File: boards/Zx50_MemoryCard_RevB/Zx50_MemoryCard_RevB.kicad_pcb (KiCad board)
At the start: 4 copper layers, 132.1 x 107.9 mm, 115 parts, among them J1 3.3V, J10 DEBUG, J2 Zx50_EdgeConnector, J3 TP_CLK, J4 TP_MCLK, J5 GND, J6 GND, J7 GND, J8 JTAG, J9 RJ45_RB1-125B8G1A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

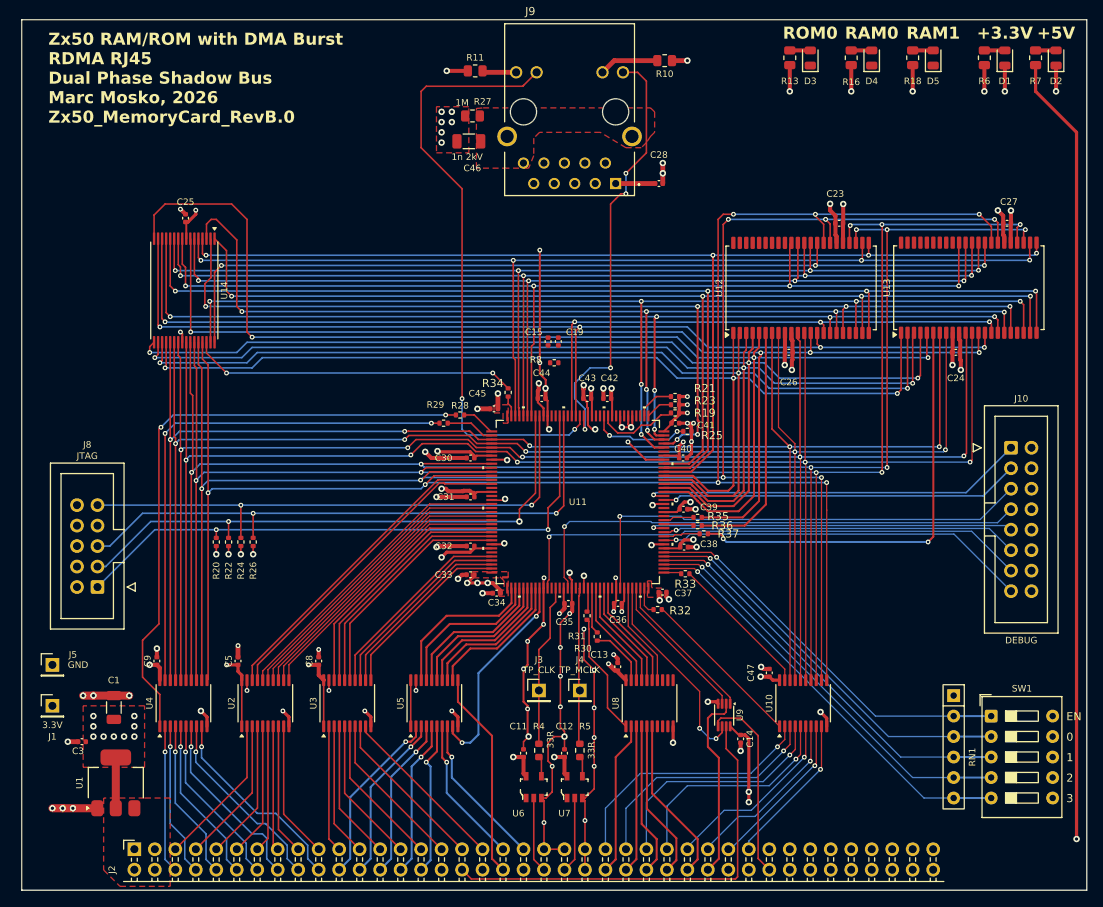
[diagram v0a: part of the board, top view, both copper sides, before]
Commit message: tweeks before refitting with quartus
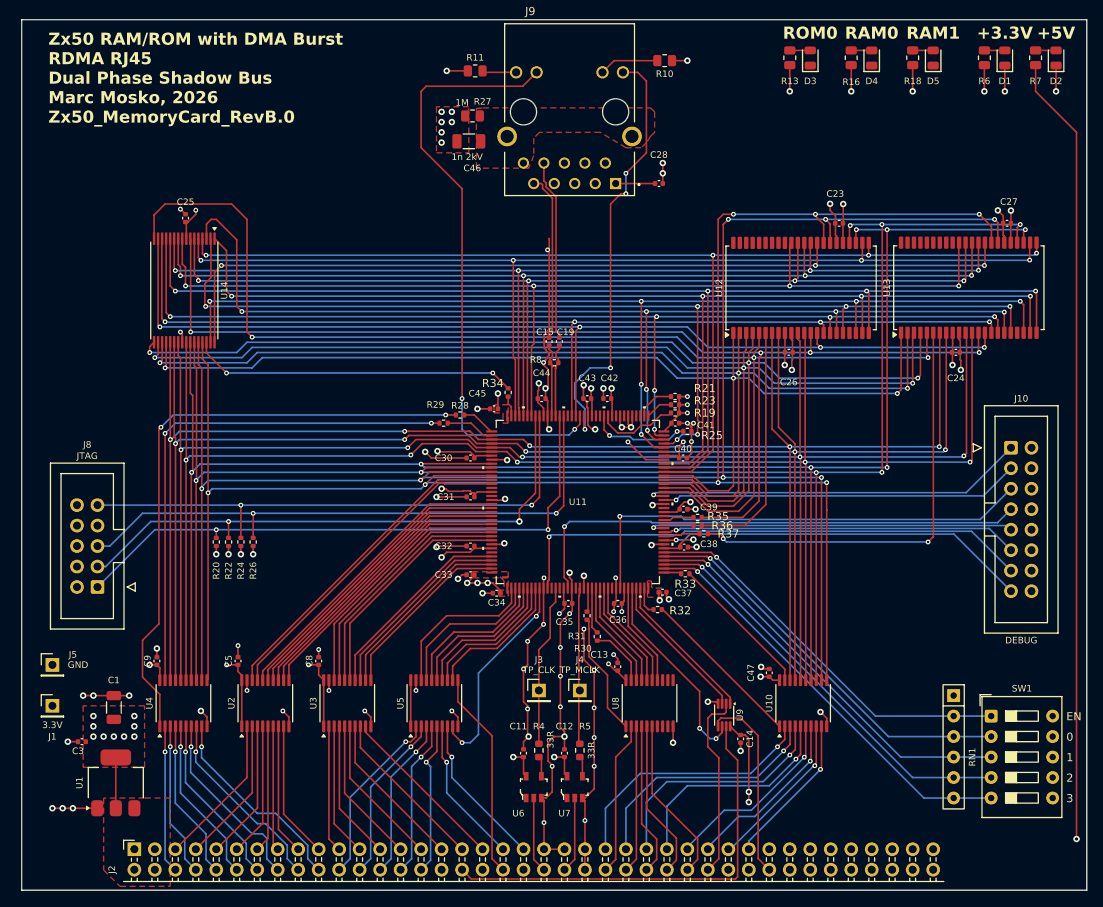
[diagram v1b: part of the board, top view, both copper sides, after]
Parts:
- moved C15 1.40 mm to (98.4, 97.1)
- moved C19 1.14 mm to (97.2, 97.1)
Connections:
- C15 pad 1: /FPGA And Memory/RX_CLK_FLT_N -> /FPGA And Memory/RX_CLK_FLT_P
- C15 pad 2: /FPGA And Memory/RX_CLK_N -> /FPGA And Memory/RX_CLK_P
- C19 pad 1: /FPGA And Memory/RX_CLK_FLT_P -> /FPGA And Memory/RX_CLK_FLT_N
- C19 pad 2: /FPGA And Memory/RX_CLK_P -> /FPGA And Memory/RX_CLK_N
- R8 pad 1: /FPGA And Memory/RX_CLK_FLT_N -> /FPGA And Memory/RX_CLK_FLT_P
- R8 pad 2: /FPGA And Memory/RX_CLK_FLT_P -> /FPGA And Memory/RX_CLK_FLT_N
- U11 pad 132: /FPGA And Memory/RX_CLK_FLT_N -> /FPGA And Memory/RX_CLK_FLT_P
- U11 pad 133: /FPGA And Memory/RX_CLK_FLT_P -> /FPGA And Memory/RX_CLK_FLT_N
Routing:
- net /FPGA And Memory/RX_CLK_P: track 0.00 -> 22.4 mm
- net /FPGA And Memory/RX_CLK_N: track 0.00 -> 20.8 mm
- net /FPGA And Memory/RX_CLK_FLT_P: track 0.00 -> 9.11 mm
- net /FPGA And Memory/RX_CLK_FLT_N: track 0.00 -> 9.11 mm
- net GND: track 247.8 -> 250.2 mm
- net +3.3V: track 156.0 -> 155.1 mm

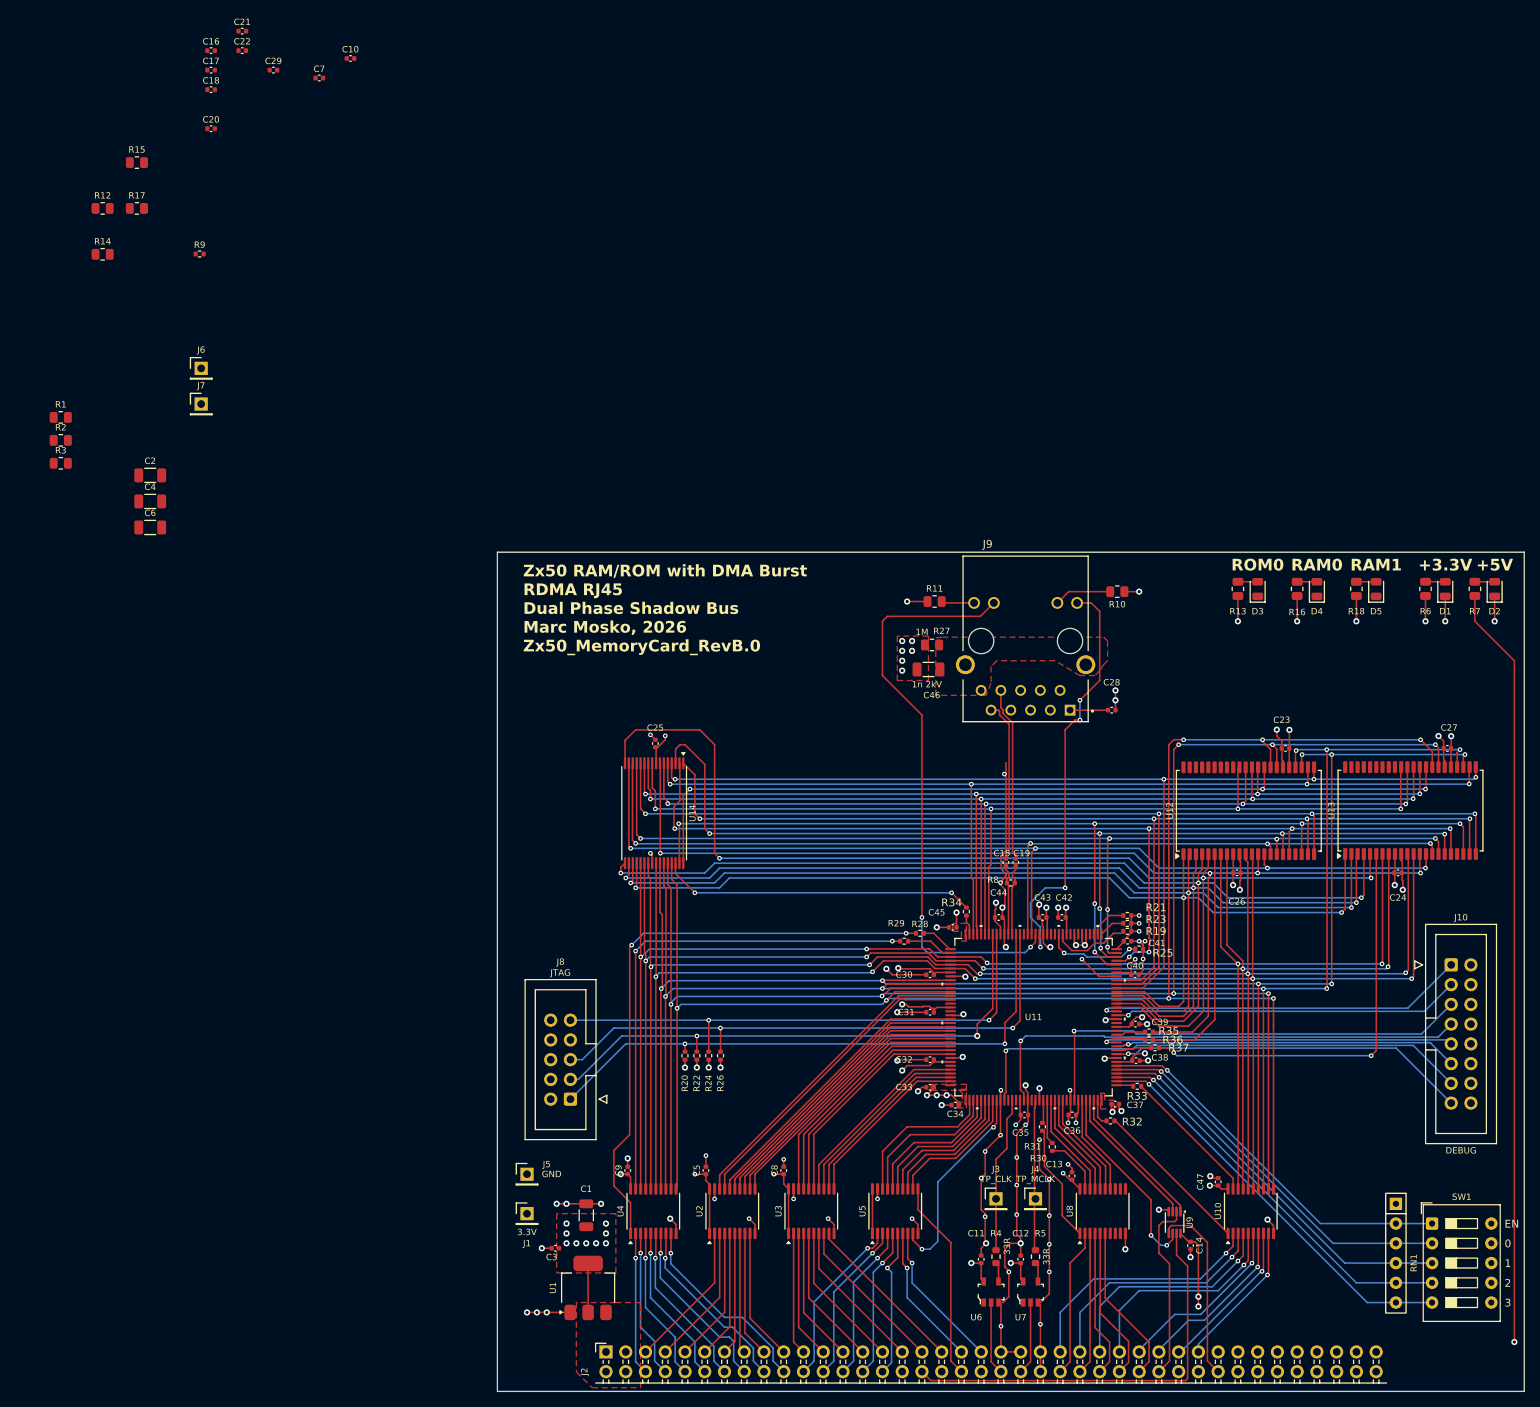
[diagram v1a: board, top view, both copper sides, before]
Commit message: more work on revb memory card, plus a diag program for rev a1.
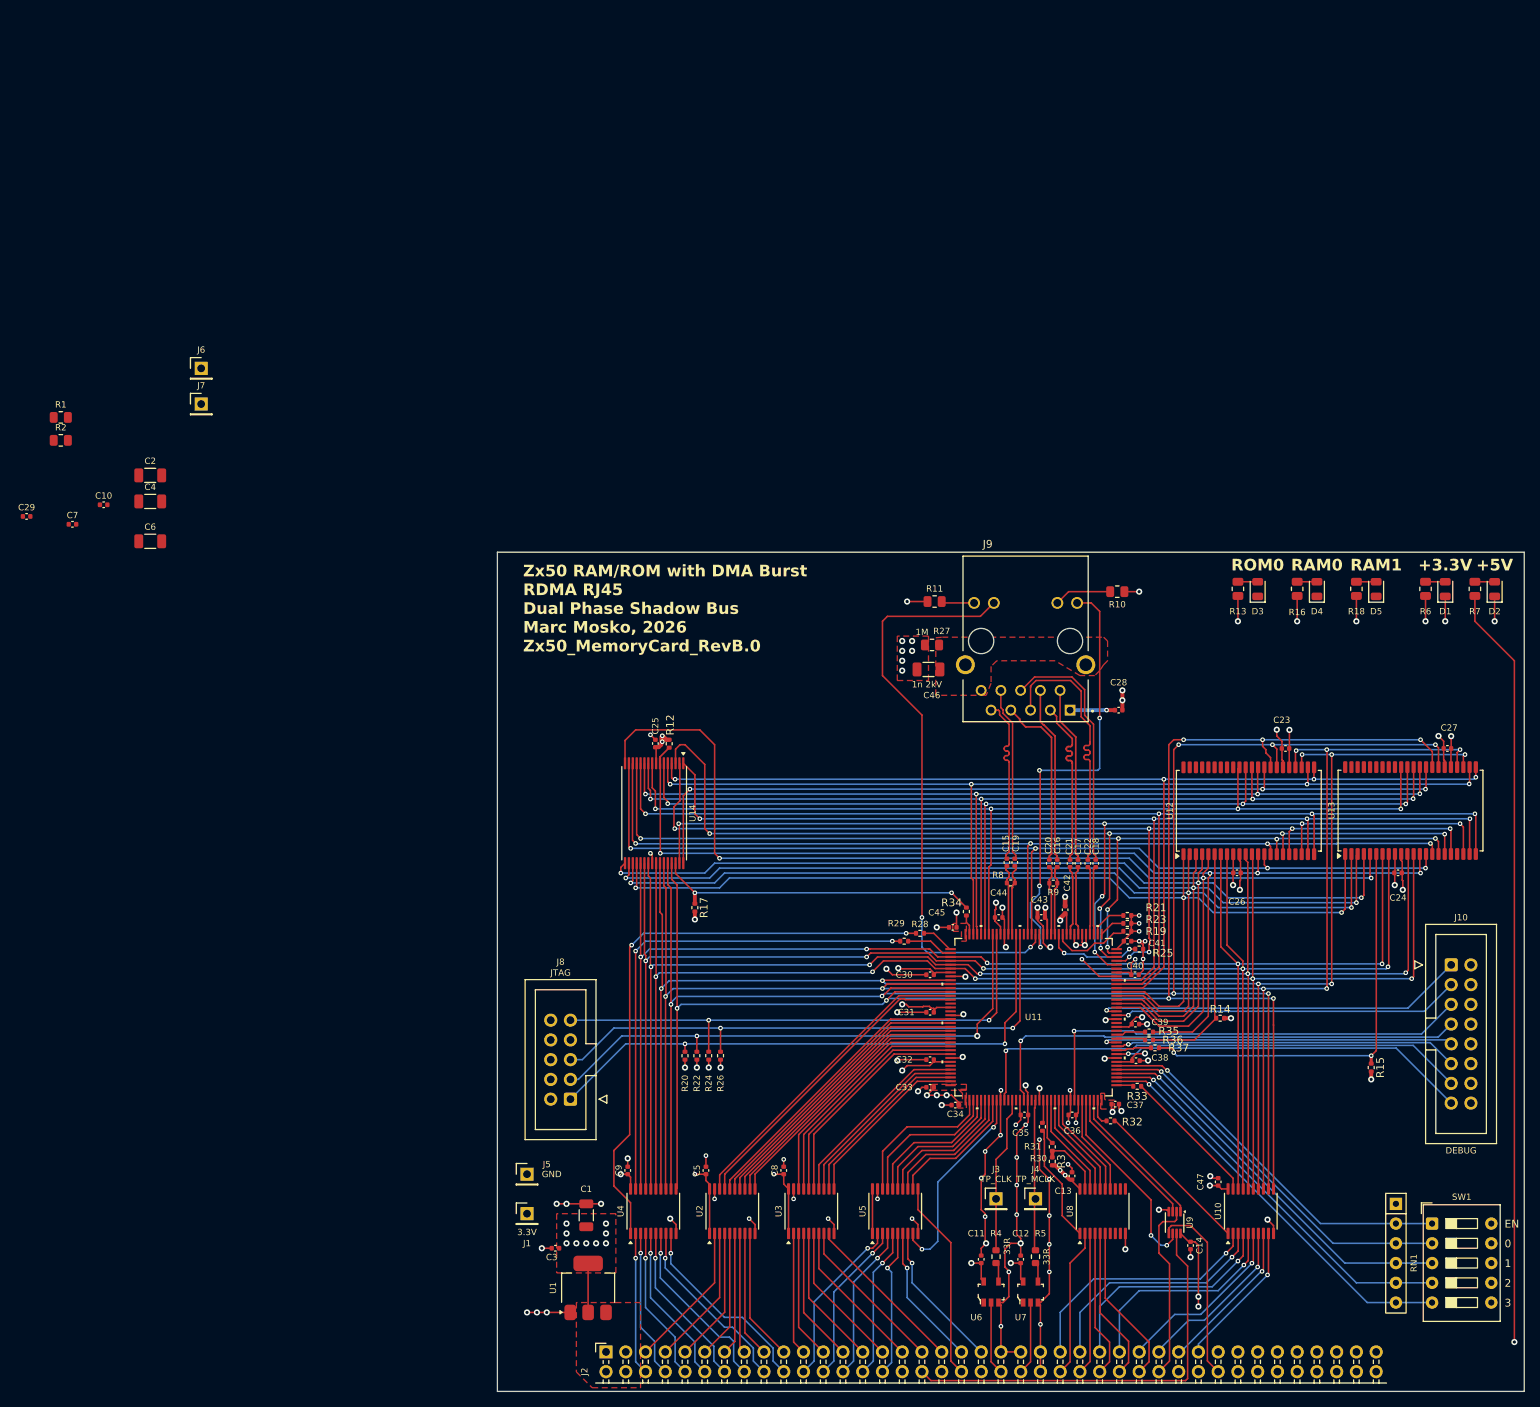
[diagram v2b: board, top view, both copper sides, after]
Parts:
- R12, R14, R15, R17, R3: footprint Resistor_SMD:R_0805_2012Metric -> Resistor_SMD:R_0402_1005Metric
- moved R15 196.9 mm to (144.1, 123.4), turned to -90 degrees
- moved R14 174.1 mm to (124.7, 117.1)
- moved R3 156.0 mm to (103.1, 135.5), turned to -90 degrees
- moved C18 151.2 mm to (108.7, 97.2), turned to 90 degrees
- moved C17 151.1 mm to (106.4, 97.2), turned to 90 degrees
- moved C21 151.0 mm to (105.4, 97.2), turned to 90 degrees
- moved C16 150.9 mm to (103.8, 97.2), turned to 90 degrees
- moved C22 150.9 mm to (107.7, 97.2), turned to 90 degrees
- moved C20 143.4 mm to (102.7, 97.2), turned to 90 degrees
- moved R9 136.4 mm to (103.3, 99.7), turned to 180 degrees
- moved R17 115.1 mm to (57.1, 102.9), turned to -90 degrees
- moved R12 100.3 mm to (53.8, 81.8), turned to 90 degrees
- moved C10 65.6 mm to (-18.9, 51.1)
- moved C29 65.6 mm to (-28.8, 52.6)
- moved C7 65.6 mm to (-22.9, 53.6)
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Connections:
- C16 pad 1: /FPGA And Memory/RX_DAT_FLT_N -> /FPGA And Memory/RX_DAT_FLT_P
- C16 pad 2: /FPGA And Memory/RX_DAT_N -> /FPGA And Memory/RX_DAT_P
- C17 pad 1: /FPGA And Memory/TX_CLK_FLT_N -> /FPGA And Memory/TX_DAT_FLT_P
- C17 pad 2: /FPGA And Memory/TX_CLK_N -> /FPGA And Memory/TX_DAT_P
- C18 pad 1: /FPGA And Memory/TX_DAT_FLT_N -> /FPGA And Memory/TX_CLK_FLT_N
- C18 pad 2: /FPGA And Memory/TX_DAT_N -> /FPGA And Memory/TX_CLK_N
- C20 pad 1: /FPGA And Memory/RX_DAT_FLT_P -> /FPGA And Memory/RX_DAT_FLT_N
- C20 pad 2: /FPGA And Memory/RX_DAT_P -> /FPGA And Memory/RX_DAT_N
- C21 pad 1: /FPGA And Memory/TX_CLK_FLT_P -> /FPGA And Memory/TX_DAT_FLT_N
- C21 pad 2: /FPGA And Memory/TX_CLK_P -> /FPGA And Memory/TX_DAT_N
- C22 pad 1: /FPGA And Memory/TX_DAT_FLT_P -> /FPGA And Memory/TX_CLK_FLT_P
- C22 pad 2: /FPGA And Memory/TX_DAT_P -> /FPGA And Memory/TX_CLK_P
- R9 pad 1: /FPGA And Memory/RX_DAT_FLT_N -> /FPGA And Memory/RX_DAT_FLT_P
- R9 pad 2: /FPGA And Memory/RX_DAT_FLT_P -> /FPGA And Memory/RX_DAT_FLT_N
- U11 pad 111: /FPGA And Memory/TX_DAT_FLT_N -> /FPGA And Memory/TX_CLK_FLT_N
- U11 pad 112: /FPGA And Memory/TX_DAT_FLT_P -> /FPGA And Memory/TX_CLK_FLT_P
- U11 pad 115: /FPGA And Memory/TX_CLK_FLT_N -> /FPGA And Memory/TX_DAT_FLT_P
- U11 pad 117: /FPGA And Memory/TX_CLK_FLT_P -> /FPGA And Memory/TX_DAT_FLT_N
- U11 pad 121: /FPGA And Memory/RX_DAT_FLT_N -> /FPGA And Memory/RX_DAT_FLT_P
- U11 pad 122: /FPGA And Memory/RX_DAT_FLT_P -> /FPGA And Memory/RX_DAT_FLT_N
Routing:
- net /FPGA And Memory/TX_CLK_P: track 0.00 -> 35.0 mm
- net /FPGA And Memory/TX_CLK_N: track 0.00 -> 32.1 mm
- net /FPGA And Memory/TX_DAT_P: track 0.00 -> 22.7 mm
- net /FPGA And Memory/RX_DAT_P: track 0.00 -> 22.7 mm
- net /FPGA And Memory/RX_DAT_N: track 0.00 -> 22.7 mm
- net /FPGA And Memory/TX_DAT_N: track 0.00 -> 22.6 mm
- net GND: track 250.2 -> 230.0 mm, vias 90 -> 88
- net /FPGA And Memory/RX_DAT_FLT_P: track 0.00 -> 9.00 mm
- net /FPGA And Memory/RX_DAT_FLT_N: track 0.00 -> 8.96 mm
- net /FPGA And Memory/TX_DAT_FLT_P: track 0.00 -> 8.88 mm
- net /FPGA And Memory/TX_DAT_FLT_N: track 0.00 -> 8.88 mm
- net /FPGA And Memory/TX_CLK_FLT_P: track 0.00 -> 8.77 mm
- net /FPGA And Memory/TX_CLK_FLT_N: track 0.00 -> 8.76 mm
- net +3.3V: track 155.1 -> 161.7 mm, vias 49 -> 54
- net /FPGA And Memory/~GRN: track 54.3 -> 56.9 mm
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
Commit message: fixup pic z80 timing.  add memory test script to pico
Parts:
- removed J7: GND, Connector_PinHeader_2.54mm:PinHeader_1x01_P2.54mm_Vertical
- added D6: YLW, LED_SMD:LED_0805_2012Metric, F.Cu at (145.4, 61.9)
- added R38: 330, Resistor_SMD:R_0805_2012Metric, F.Cu at (142.9, 61.9)
- added R39: 33, Resistor_SMD:R_0402_1005Metric, F.Cu at (118.4, 123.2)
- C29: moved to B.Cu
- moved R2 171.9 mm to (120.5, 135.1), turned to 180 degrees
- moved J6 160.7 mm to (149.6, 72.1)
- moved C10 130.8 mm to (79.8, 136.9), turned to 90 degrees
- moved C2 126.8 mm to (38.5, 163.2), turned to 180 degrees
- moved C7 122.6 mm to (48.3, 153.4), turned to 90 degrees
- moved C4 121.5 mm to (38.5, 160.7), turned to 180 degrees
- moved C6 114.6 mm to (38.5, 158.1), turned to 180 degrees
- moved C29 98.9 mm to (37.1, 126.3), turned to -90 degrees
- moved R1 96.4 mm to (47.3, 104.1), turned to 180 degrees
- moved R16 8.26 mm to (126.4, 61.9)
- moved D3 8.25 mm to (121.3, 61.9)
- moved D4 8.25 mm to (128.9, 61.9)
- moved D5 8.25 mm to (136.5, 61.9)
- moved R13 8.25 mm to (118.7, 61.9)
- moved R18 8.25 mm to (134.0, 61.9)
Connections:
- RN1 pad 6: /CARD_A3 -> Net-(RN1-R5)
- SW1 pad 5: /CARD_A3 -> Net-(RN1-R5)
- U11 pad 48: /FPGA And Memory/~LED2 -> /FPGA And Memory/~LED0
- U11 pad 50: unconnected-(U11A-PB9B-Pad50) -> /FPGA And Memory/~LED1
- U11 pad 54: unconnected-(U11A-PB11D-Pad54) -> /FPGA And Memory/~LED2
- U11 pad 56: GND -> /FPGA And Memory/~LED3
- U11 pad 74: /CARD_A3 -> /CARD_A2
- U11 pad 75: /CARD_A2 -> /CARD_A1
- U11 pad 76: /CARD_A1 -> /CARD_A0
- U11 pad 77: /CARD_A0 -> /~BOOT_EN
- U11 pad 78: /~BOOT_EN -> Net-(U11B-PR9C)
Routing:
- net /FPGA And Memory/~LED3: track 0.00 -> 167.4 mm, vias 0 -> 4
- net /FPGA And Memory/~LED2: track 0.00 -> 158.7 mm, vias 0 -> 4
- net /FPGA And Memory/~LED1: track 0.00 -> 150.4 mm, vias 0 -> 4
- net /FPGA And Memory/~LED0: track 0.00 -> 141.9 mm, vias 0 -> 4
- net /FPGA And Memory/~OE: track 110.2 -> 164.6 mm, vias 3 -> 6
- net /CARD_A3: track 52.4 -> 0.00 mm, vias 1 -> 0
- net +3.3V: track 161.7 -> 175.6 mm, vias 54 -> 58
- net GND: track 230.0 -> 220.1 mm, vias 88 -> 100
- net Net-(U11B-PR9C): track 0.00 -> 6.57 mm
- net /~Z80_D_OE: track 64.9 -> 69.7 mm
- net Net-(RN1-R5): track 0.00 -> 4.66 mm
- net Net-(D6-A): track 0.00 -> 2.54 mm
- net /~SH_D_OE: track 18.1 -> 20.5 mm
- net /~BOOT_EN: track 49.0 -> 49.7 mm
- net /FPGA And Memory/L_A9: track 135.8 -> 135.7 mm, vias 6 -> 4
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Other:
- board text added: "LED0"
- board text added: "LED1"
- board text added: "LED2"
- board text added: "LED3"
- board text removed: "RAM0"
- board text removed: "RAM1"
- board text removed: "ROM0"
